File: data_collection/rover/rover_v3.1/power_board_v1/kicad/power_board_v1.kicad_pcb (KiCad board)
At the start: 2 copper layers, 90 x 65 mm, 131 parts, among them J1 XT60_BATT, J10 from Pi USB2, J11 UPDI prog (UPDI/3V3/GND), J12 XT30 fallback pads, J2 PANEL_SW, J3 USB4105-GF-A (TH shell), J4 USB_A radio1, J5 USB_A radio2, J6 AUX 5V 2A, J7 PI GPIO harness, J8 AUX_CTL out (JST-GH), J9 from Pi USB1, Q2 CSD18543Q3A diode, Q3 CSD18543Q3A switch, U1 LM5145 rail A, U2 LM5145 rail B, U3 ATtiny816 (VQFN), U4 LM74800-Q1, U5 INA226 (addr 0x40), U6 TPS7A1633 3V3 60V LDO, U7 TPS2553 1.7A, U8 TPS2553 1.7A, U9 AP2112K-3.3 (switched)

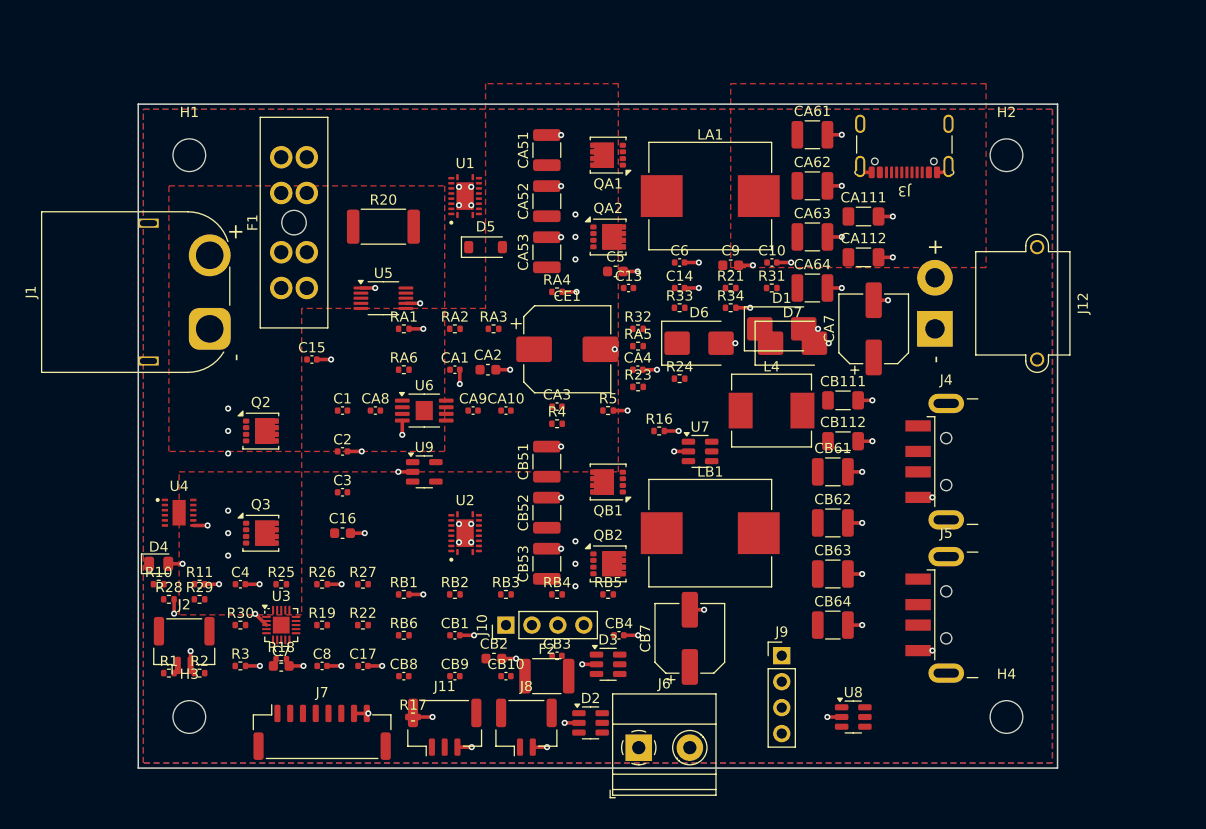
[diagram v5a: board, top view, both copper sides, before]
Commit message: Routing milestone: 809 segments + 89 vias via freerouting pipeline (DSN class injection, xvfb headless, SES parser); 68 GND stitch vias; 3 F.Cu power pours; 136/221 pairs routed, 85 residual for interactive session; DRC baseline committed; AUDIT PASS
Co-Authored-By: Claude Fable 5 <noreply@anthropic.com>
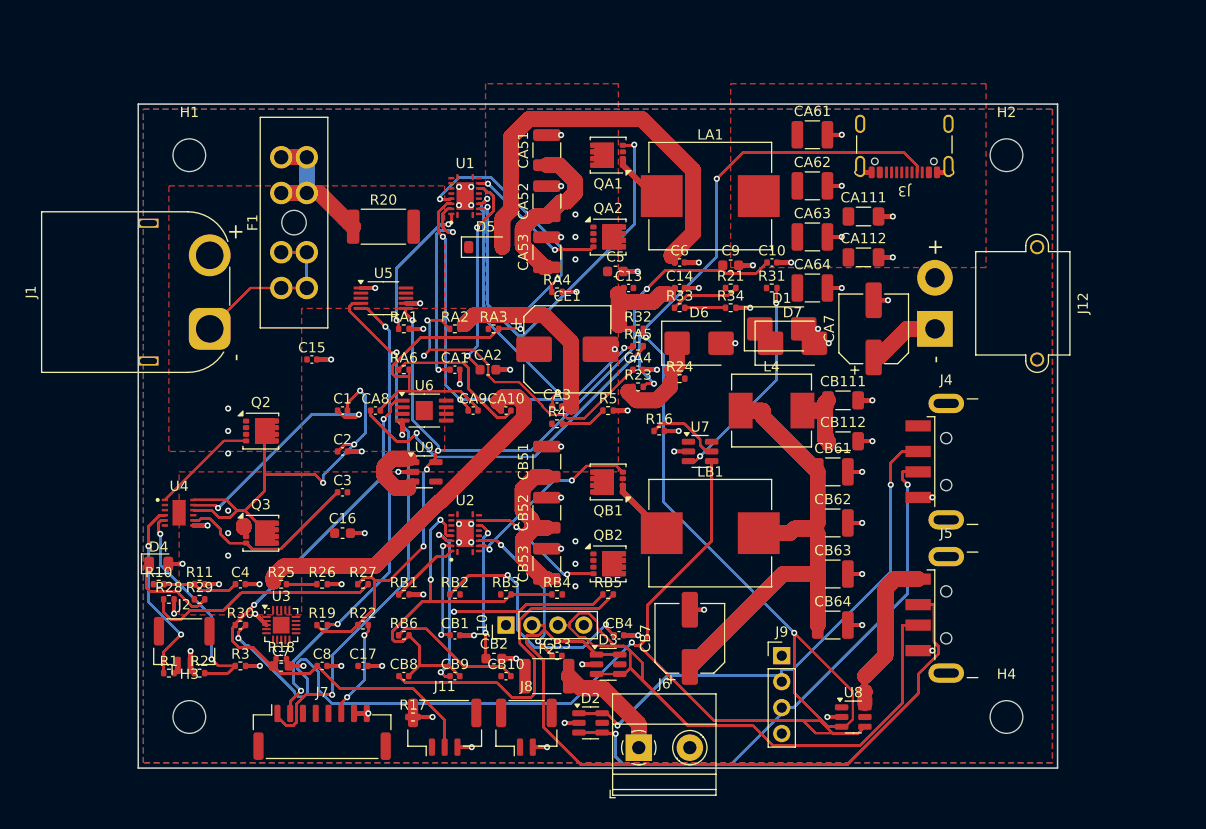
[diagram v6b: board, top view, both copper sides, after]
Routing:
- net GND: track 101.0 -> 1576.1 mm
- net FAULT_USB: track 0.00 -> 762.8 mm, vias 0 -> 2
- net 3V3_SW: track 0.00 -> 631.5 mm, vias 0 -> 5
- net D2_N: track 0.00 -> 591.9 mm
- net MCU_3V3: track 0.00 -> 464.9 mm, vias 0 -> 2
- net FB_A: track 0.00 -> 463.4 mm, vias 0 -> 3
- net D1_P: track 0.00 -> 447.9 mm, vias 0 -> 2
- net SDA: track 0.00 -> 427.1 mm, vias 0 -> 2
- net D2_P: track 0.00 -> 420.1 mm
- net D1_N: track 0.00 -> 416.4 mm, vias 0 -> 2
- net 5V_A: track 0.00 -> 411.8 mm
- net SCL: track 0.00 -> 378.4 mm, vias 0 -> 3
- net CC1_A: track 0.00 -> 374.6 mm, vias 0 -> 2
- net EN_USB2: track 0.00 -> 359.1 mm, vias 0 -> 2
- net 5VB_PRE: track 0.00 -> 350.5 mm
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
